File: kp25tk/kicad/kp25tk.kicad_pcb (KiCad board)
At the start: 2 copper layers, 66 parts, among them J1 Host Connector, J2 Wire Wrap Connector, J3 Power In, J4 Row Select In, J5 Column Out, J6 NMI Out, J7 Reset Out, J8 Mode Out, SW0 KEY00, SW1 KEY01, SW10 KEY0A, SW11 KEY0B, SW12 KEY0C, SW13 KEY0D, SW14 KEY0E, SW15 KEY0F, SW16 KEY10, SW17 KEY11, SW18 KEY12, SW19 KEY13, SW2 KEY02, SW20 KEY14, SW21 KEY15, SW22 KEY16, SW23 KEY17, SW24 NMI, SW25 RESET, SW27 SWITCH, SW3 KEY03, SW4 KEY04, SW5 KEY05, SW6 KEY06, SW7 KEY07, SW8 KEY08, SW9 KEY09, U1 74LS14

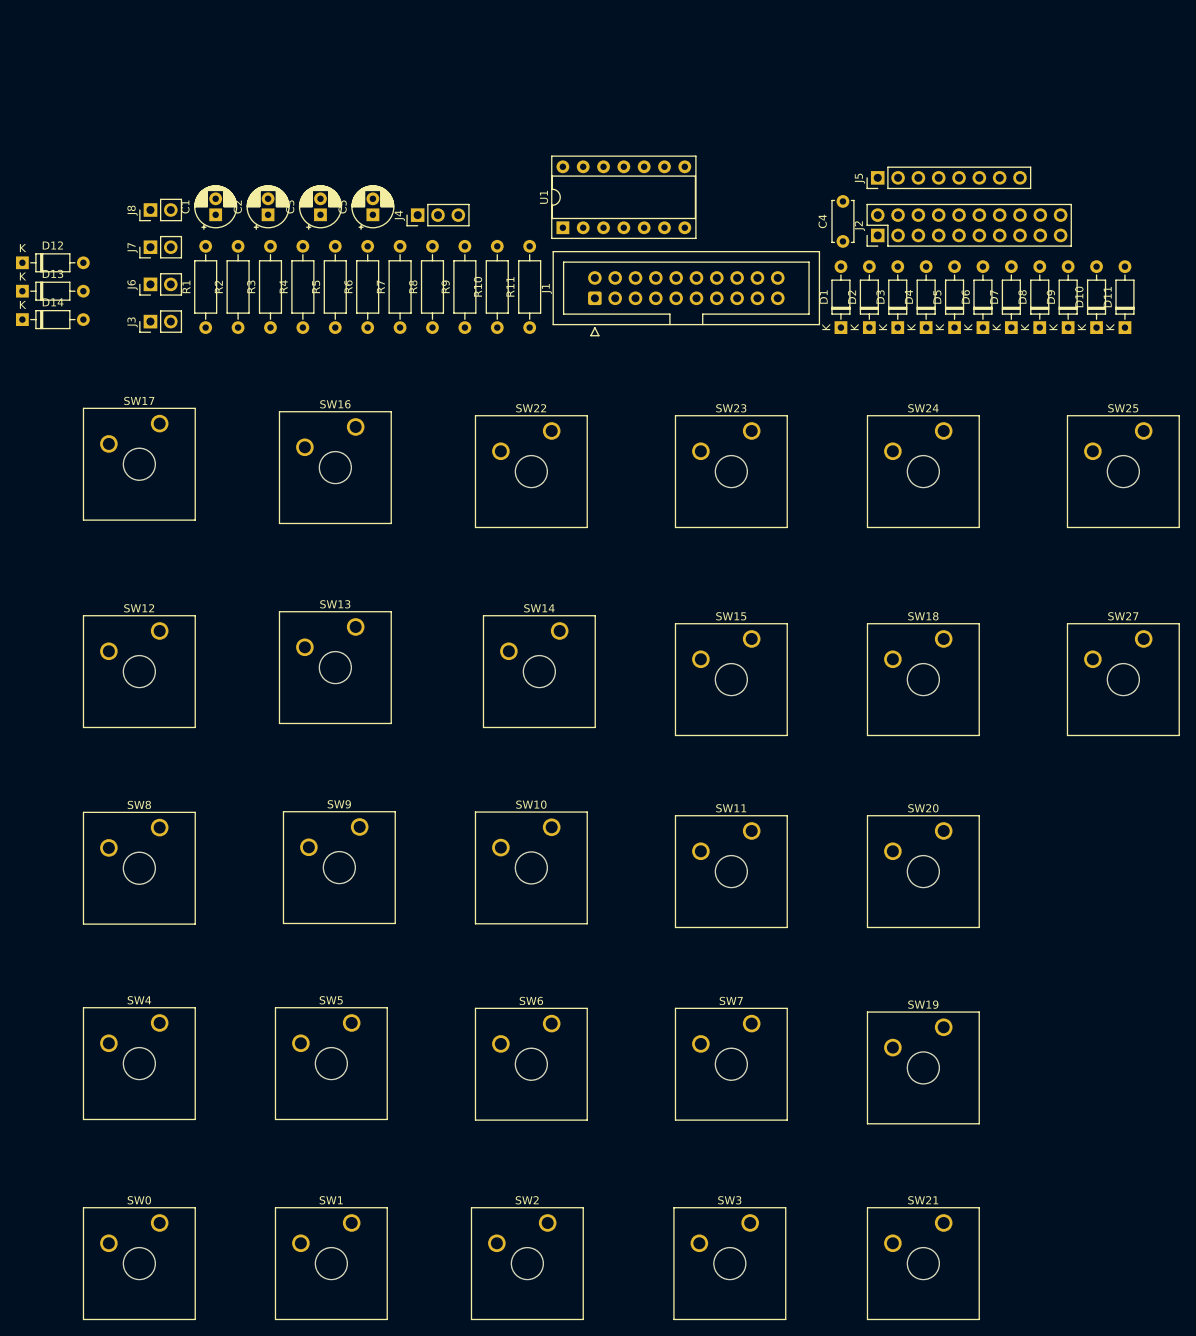
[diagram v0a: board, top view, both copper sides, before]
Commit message: kp25tk/: Many fixes, and much better and smaller PCB layout (incomplete)
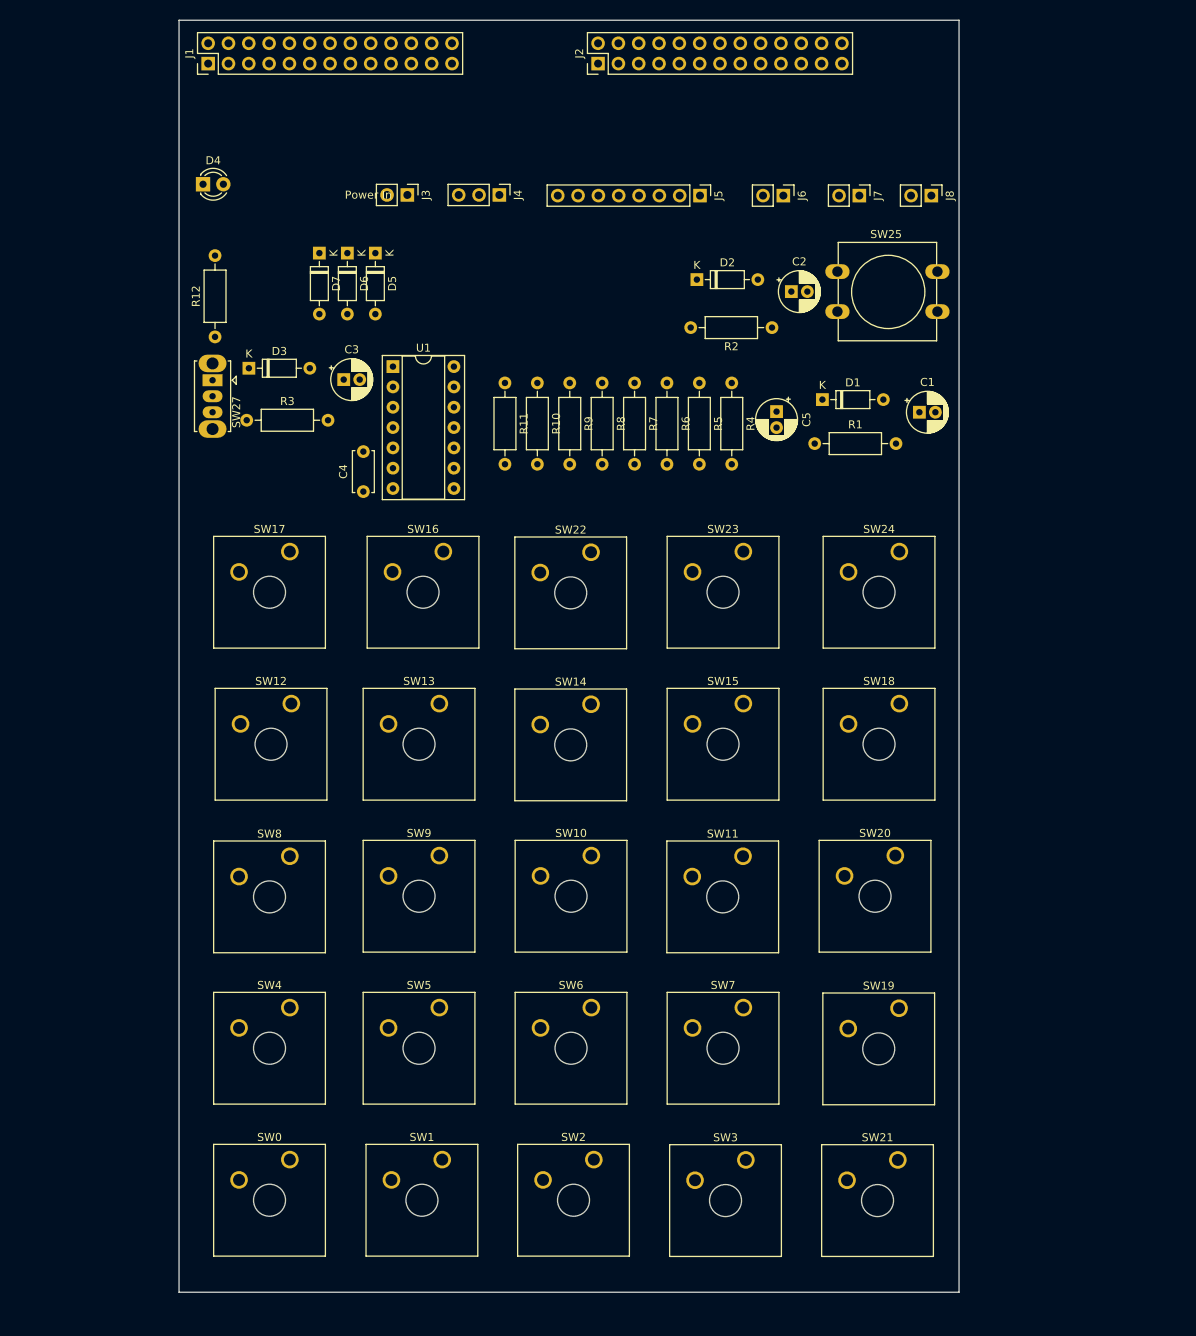
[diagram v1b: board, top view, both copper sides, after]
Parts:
- removed D10, D11, D12, D13, D14, D8, D9: 1N4148, Diode_THT:D_DO-35_SOD27_P7.62mm_Horizontal
- added R12: 1K5, Resistor_THT:R_Axial_DIN0207_L6.3mm_D2.5mm_P10.16mm_Horizontal, F.Cu at (50.5, 64.2)
- D4: value 1N4148 -> LED; footprint Diode_THT:D_DO-35_SOD27_P7.62mm_Horizontal -> LED_THT:LED_D3.0mm
- J1: footprint Connector_IDC:IDC-Header_2x10_P2.54mm_Vertical -> Connector_PinHeader_2.54mm:PinHeader_2x13_P2.54mm_Vertical
- J2: value Wire Wrap Connector -> Config Header; footprint Connector_PinHeader_2.54mm:PinHeader_2x10_P2.54mm_Vertical -> Connector_PinHeader_2.54mm:PinHeader_2x13_P2.54mm_Vertical
- J8: value Mode Out -> Switch
- SW25: footprint Button_Switch_Keyboard:SW_Cherry_MX_1.00u_Plate -> Button_Switch_THT:SW_PUSH-12mm
- SW27: footprint Button_Switch_Keyboard:SW_Cherry_MX_1.00u_Plate -> Button_Switch_THT:SW_Slide_1P2T_CK_OS102011MS2Q
- moved SW27 120.8 mm to (50.1, 69.6), turned to -90 degrees
- moved J8 97.6 mm to (140.0, 46.5), turned to -90 degrees
- moved D4 92.1 mm to (49.0, 45.1), turned to 0 degrees
- moved C1 91.4 mm to (138.5, 73.6), turned to 0 degrees
- moved J7 88.8 mm to (131.0, 46.5), turned to -90 degrees
- moved D7 87.0 mm to (63.5, 53.7), turned to -90 degrees
- moved D3 81.3 mm to (54.7, 68.1), turned to 0 degrees
- moved D6 80.0 mm to (67.0, 53.7), turned to -90 degrees
- moved J6 79.9 mm to (121.5, 46.5), turned to -90 degrees
- moved R1 77.5 mm to (125.4, 77.5), turned to 0 degrees
- moved D5 73.0 mm to (70.5, 53.7), turned to -90 degrees
- moved C4 67.6 mm to (69.0, 83.5)
- moved R2 66.7 mm to (120.1, 63.0), turned to 180 degrees
- moved C2 66.1 mm to (122.5, 58.5), turned to 0 degrees
- moved J1 56.5 mm to (49.6, 30.0)
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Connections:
- D4 pad 1: Net-(D4-K) -> Earth
- J4 pad 1: Net-(D14-K) -> Net-(D5-K)
- J4 pad 2: Net-(D13-K) -> Net-(D6-K)
- J4 pad 3: Net-(D12-K) -> Net-(D7-K)
- J5 pad 1: Net-(D4-K) -> Net-(J5-~{COL0})
- J5 pad 2: Net-(D5-K) -> Net-(J5-~{COL1})
- J5 pad 3: Net-(D6-K) -> Net-(J5-~{COL2})
- J5 pad 4: Net-(D7-K) -> Net-(J5-~{COL3})
- J5 pad 5: Net-(D8-K) -> Net-(J5-~{COL4})
- J5 pad 6: Net-(D9-K) -> Net-(J5-~{COL5})
- J5 pad 7: Net-(D10-K) -> Net-(J5-~{COL6})
- J5 pad 8: Net-(D11-K) -> Net-(J5-~{COL7})
- R10 pad 1: Net-(D10-A) -> Net-(J5-~{COL6})
- R11 pad 1: Net-(D11-A) -> Net-(J5-~{COL7})
- R4 pad 1: Net-(D4-A) -> Net-(J5-~{COL0})
- R5 pad 1: Net-(D5-A) -> Net-(J5-~{COL1})
- R6 pad 1: Net-(D6-A) -> Net-(J5-~{COL2})
- R7 pad 1: Net-(D7-A) -> Net-(J5-~{COL3})
- R8 pad 1: Net-(D8-A) -> Net-(J5-~{COL4})
- R9 pad 1: Net-(D9-A) -> Net-(J5-~{COL5})
- SW0 pad 1: Net-(D4-A) -> Net-(J5-~{COL0})
- SW0 pad 2: Net-(D14-A) -> Net-(D5-A)
- SW1 pad 1: Net-(D5-A) -> Net-(J5-~{COL1})
- SW1 pad 2: Net-(D14-A) -> Net-(D5-A)
- SW10 pad 1: Net-(D6-A) -> Net-(J5-~{COL2})
- SW10 pad 2: Net-(D13-A) -> Net-(D6-A)
- SW11 pad 1: Net-(D7-A) -> Net-(J5-~{COL3})
- SW11 pad 2: Net-(D13-A) -> Net-(D6-A)
- SW12 pad 1: Net-(D8-A) -> Net-(J5-~{COL4})
- SW12 pad 2: Net-(D13-A) -> Net-(D6-A)
- SW13 pad 1: Net-(D9-A) -> Net-(J5-~{COL5})
- SW13 pad 2: Net-(D13-A) -> Net-(D6-A)
- SW14 pad 1: Net-(D10-A) -> Net-(J5-~{COL6})
- SW14 pad 2: Net-(D13-A) -> Net-(D6-A)
- SW15 pad 1: Net-(D11-A) -> Net-(J5-~{COL7})
- SW15 pad 2: Net-(D13-A) -> Net-(D6-A)
- SW16 pad 1: Net-(D4-A) -> Net-(J5-~{COL0})
- SW16 pad 2: Net-(D12-A) -> Net-(D7-A)
- SW17 pad 1: Net-(D5-A) -> Net-(J5-~{COL1})
- SW17 pad 2: Net-(D12-A) -> Net-(D7-A)
- SW18 pad 1: Net-(D6-A) -> Net-(J5-~{COL2})
- SW18 pad 2: Net-(D12-A) -> Net-(D7-A)
- SW19 pad 1: Net-(D7-A) -> Net-(J5-~{COL3})
- SW19 pad 2: Net-(D12-A) -> Net-(D7-A)
- SW2 pad 1: Net-(D6-A) -> Net-(J5-~{COL2})
- SW2 pad 2: Net-(D14-A) -> Net-(D5-A)
- SW20 pad 1: Net-(D8-A) -> Net-(J5-~{COL4})
- SW20 pad 2: Net-(D12-A) -> Net-(D7-A)
- SW21 pad 1: Net-(D9-A) -> Net-(J5-~{COL5})
- SW21 pad 2: Net-(D12-A) -> Net-(D7-A)
- SW22 pad 1: Net-(D10-A) -> Net-(J5-~{COL6})
- SW22 pad 2: Net-(D12-A) -> Net-(D7-A)
- SW23 pad 1: Net-(D11-A) -> Net-(J5-~{COL7})
- SW23 pad 2: Net-(D12-A) -> Net-(D7-A)
- SW3 pad 1: Net-(D7-A) -> Net-(J5-~{COL3})
- SW3 pad 2: Net-(D14-A) -> Net-(D5-A)
- SW4 pad 1: Net-(D8-A) -> Net-(J5-~{COL4})
- SW4 pad 2: Net-(D14-A) -> Net-(D5-A)
- SW5 pad 1: Net-(D9-A) -> Net-(J5-~{COL5})
- SW5 pad 2: Net-(D14-A) -> Net-(D5-A)
- SW6 pad 1: Net-(D10-A) -> Net-(J5-~{COL6})
- SW6 pad 2: Net-(D14-A) -> Net-(D5-A)
- SW7 pad 1: Net-(D11-A) -> Net-(J5-~{COL7})
- SW7 pad 2: Net-(D14-A) -> Net-(D5-A)
- SW8 pad 1: Net-(D4-A) -> Net-(J5-~{COL0})
- SW8 pad 2: Net-(D13-A) -> Net-(D6-A)
- SW9 pad 1: Net-(D5-A) -> Net-(J5-~{COL1})
- SW9 pad 2: Net-(D13-A) -> Net-(D6-A)
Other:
- board outline added: 97.5 x 159 mm
- board text added: "KP25TK"

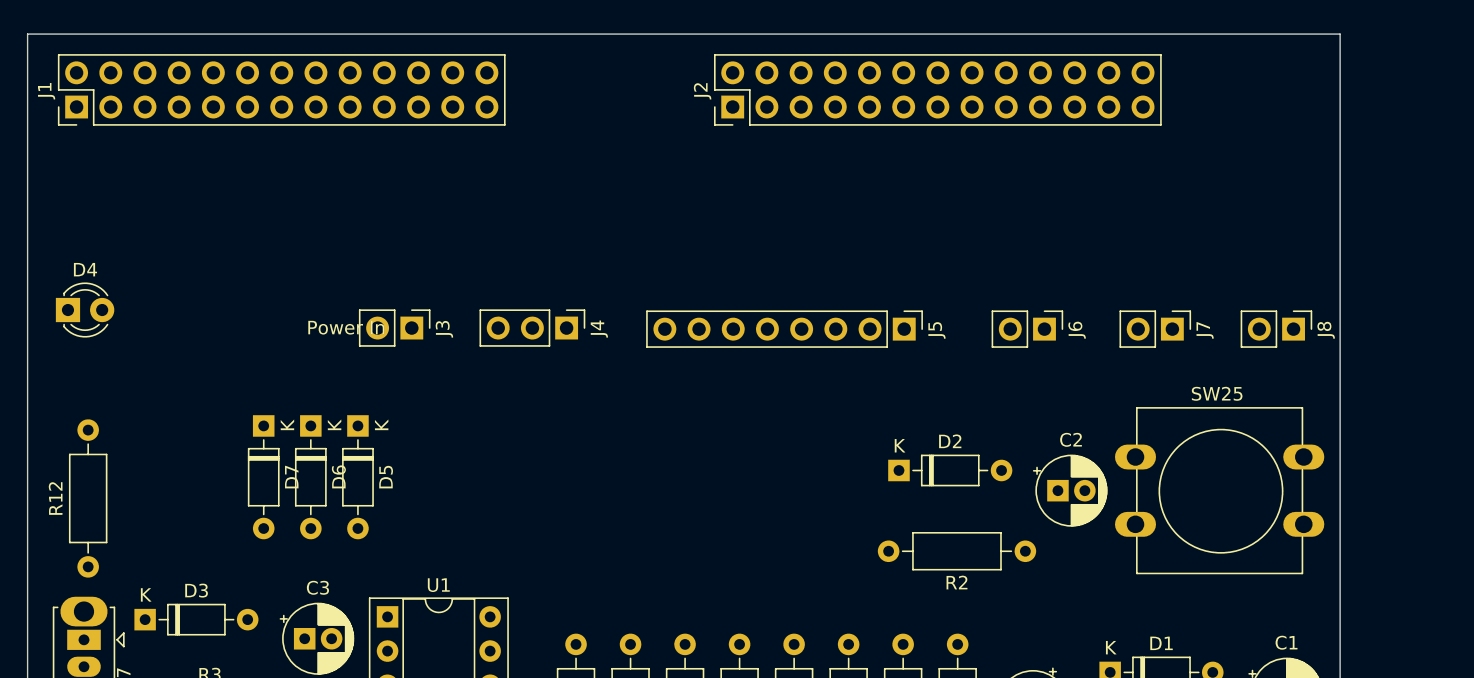
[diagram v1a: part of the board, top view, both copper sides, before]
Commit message: kp25tk/ PCB: U-shaped config area; other cleanup
- Configuration area is compactified by moving slide switch and reset
  outputs to the right of the config header, and power in to the left, and
  orienting these vertically.
- Host Conector and Config Header were upside down; rotate them 180° so
  that pin 1 is on the right instead of the left.
- Make silkscreen names "Host Connector" and "Config Header" horizontal.
- Move power LED and its resistor up.
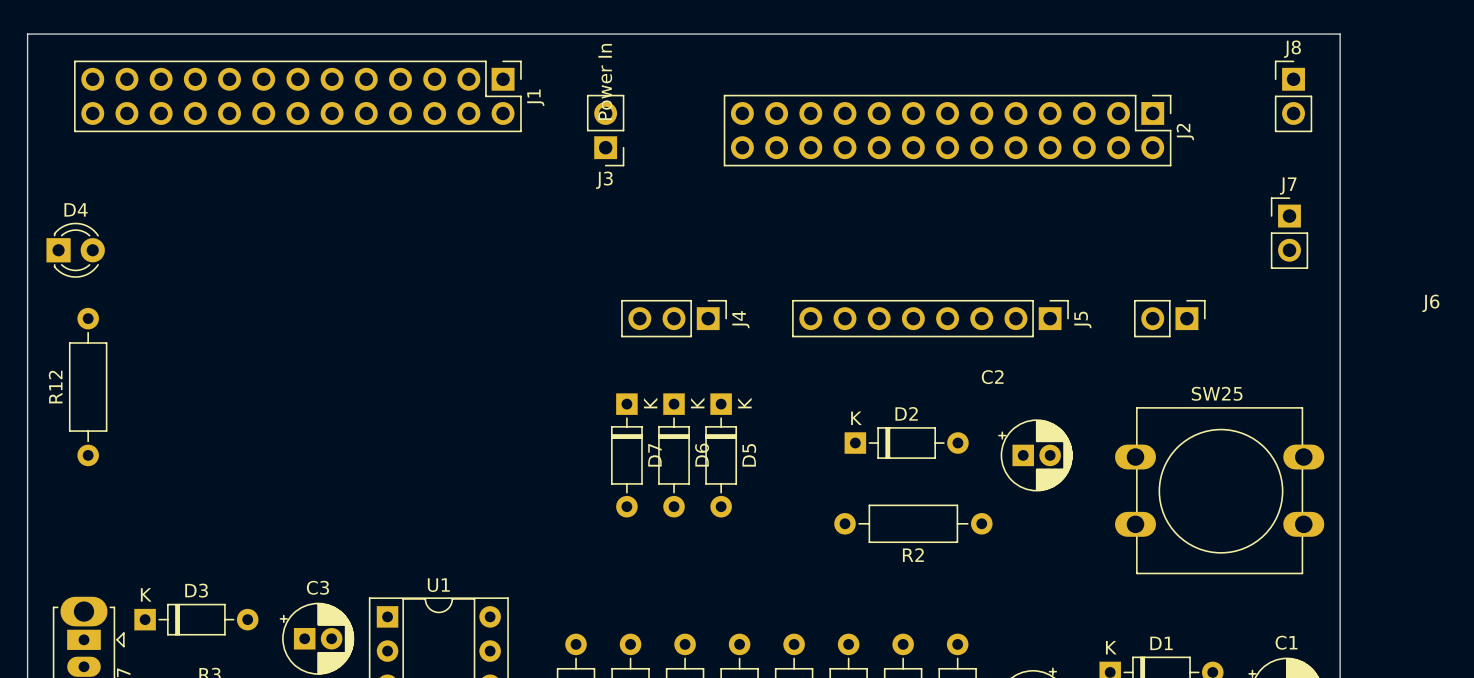
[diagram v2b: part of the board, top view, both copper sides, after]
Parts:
- moved J1 31.7 mm to (81.3, 27.9), turned to -90 degrees
- moved J2 31.2 mm to (129.5, 30.5), turned to -90 degrees
- moved D5 27.0 mm to (97.5, 52.1)
- moved D6 27.0 mm to (94.0, 52.1)
- moved D7 27.0 mm to (90.5, 52.1)
- moved J3 19.7 mm to (88.9, 33.0), turned to 180 degrees
- moved J8 18.6 mm to (140.0, 27.9), turned to 0 degrees
- moved J7 12.1 mm to (139.7, 38.1), turned to 0 degrees
- moved J5 10.9 mm to (121.9, 45.7)
- moved J6 10.6 mm to (132.1, 45.7)
- moved J4 10.5 mm to (96.5, 45.7)
- moved R12 8.28 mm to (50.5, 55.9)
- moved D4 4.49 mm to (48.3, 40.6)
- moved D2 3.83 mm to (107.5, 55.0)
- moved R2 3.83 mm to (116.8, 61.0)
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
